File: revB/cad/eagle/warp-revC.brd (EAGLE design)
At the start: 46.7 x 72.8 mm, 176 parts, among them J3 QIIC connector, J4 DF40FC-20DP-0.4V(51)

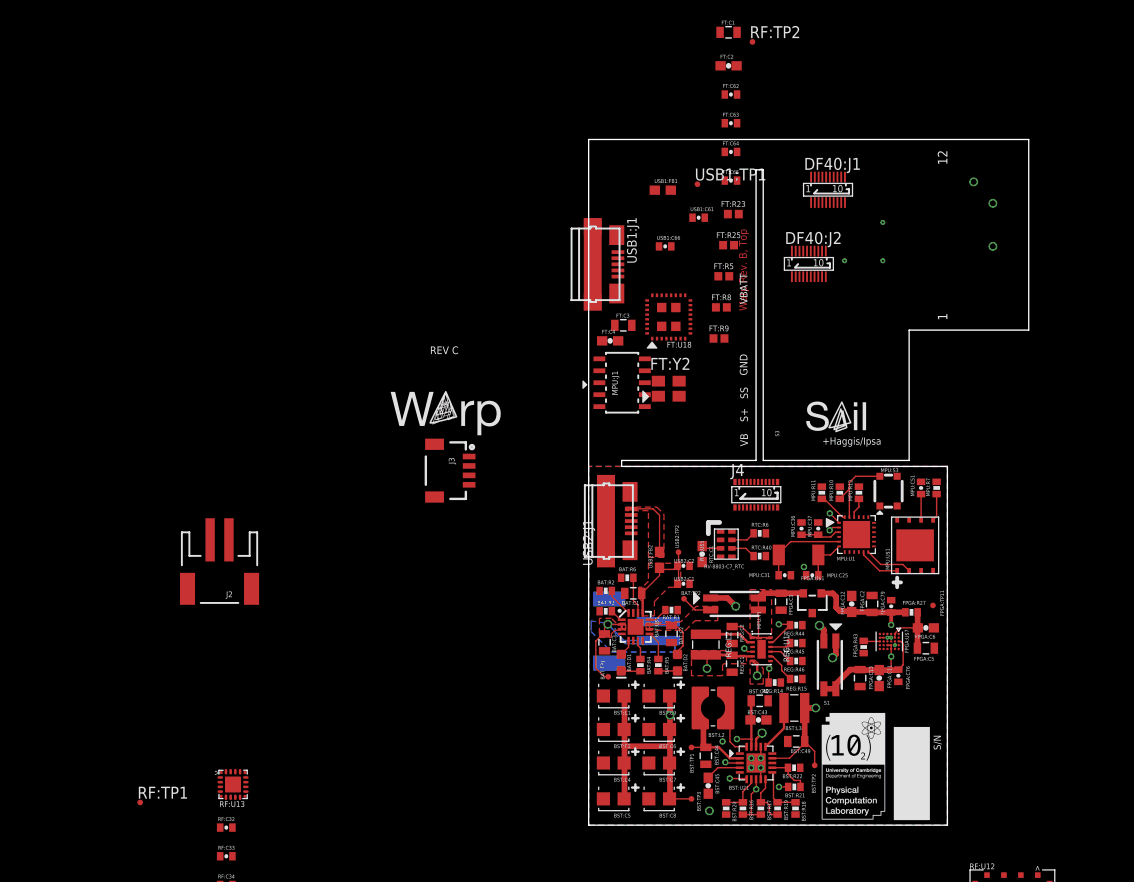
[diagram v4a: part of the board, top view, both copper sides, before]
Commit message: Top layout removed USE SPI IC
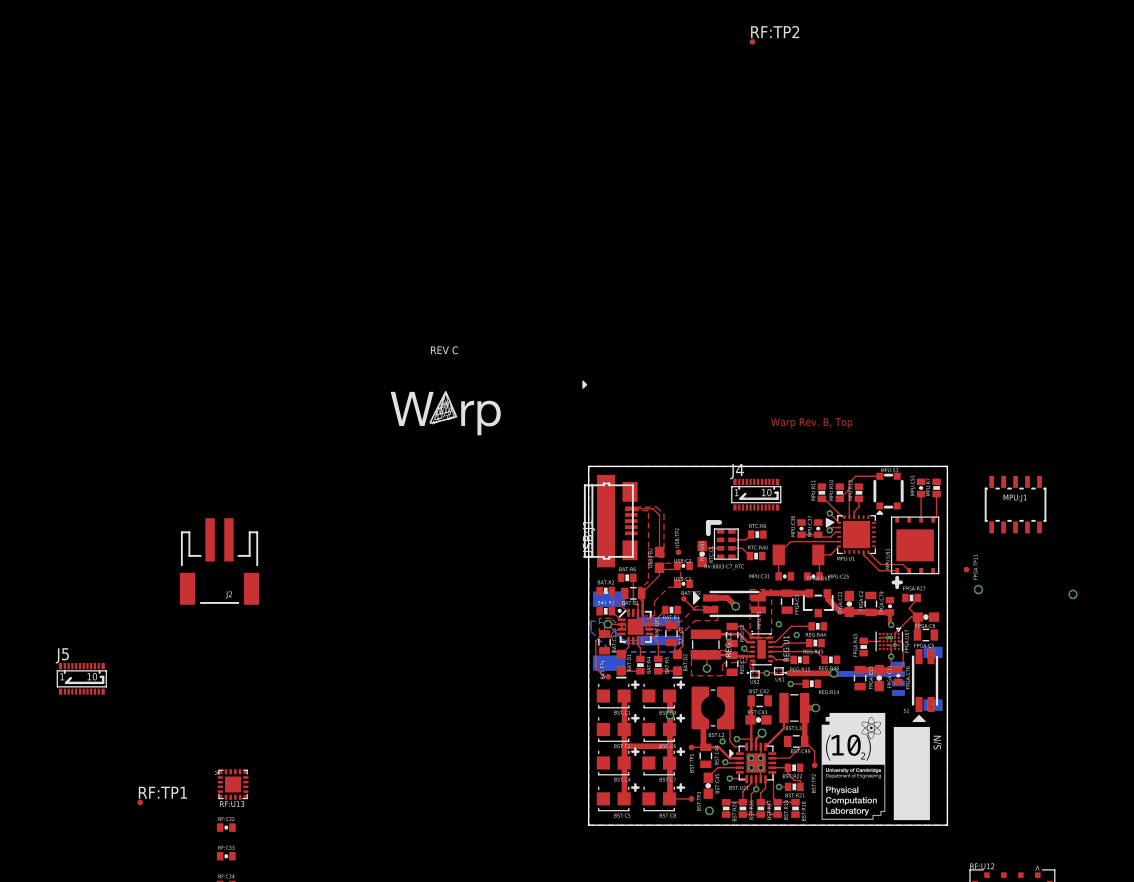
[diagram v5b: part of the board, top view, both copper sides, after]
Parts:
- removed DF40:J1, DF40:J2: DF40FC-20DP-0.4V(51)SOCKET, DF40C-20DS-0.4V(51):DF40C-20DP-0.4V(51)
- removed FT:C1, FT:C3: 4.7uF, SparkFun-Passives:0805
- removed FT:C2, FT:C4: 0.1uF, SparkFun-Passives:0603-CAP
- removed FT:C62: 0.47uF, SparkFun-Passives:0402-CAP
- removed FT:C63: 100pF, SparkFun-Passives:0402-CAP
- removed FT:C64, FT:C65: 27pF, SparkFun-Passives:0402-CAP
- removed FT:R23, FT:R25, FT:R5, FT:R8, FT:R9: (no value), SparkFun-Resistors:0402
- removed FT:U18: FT4222H, FT4222H:FT4222H
- removed FT:Y2: CS325, CS325:CS325
- removed USB1:C61: 4.7uF (pol), SparkFun-Passives:0402-CAP
- removed USB1:C66: 0.1uF, SparkFun-Passives:0402-CAP
- removed USB1:FB1: 600R/1A, SparkFun-Passives:0603
- removed USB1:J1: J_USB_MICROAB_HIROSE_ZX62-AB-5PA, j_usb_hirose_zx62-ab-5pa:J_USB_MICROAB_HIROSE_ZX62-AB-5PA
- removed USB1:TP1: TPSTP06R, testpad:TP06R
- added J5: DF40FC-20DP-0.4V(51), DF40FC-20DP-0.4V(51):DF40C-20DP-0.4V(51)
- added U$1, U$2: MAX40200, MAX40200:DSBGA
- moved J3 50.7 mm to (32.9, 15.6), flipped to the bottom
- moved MPU:J1 43.7 mm to (45.3, 34.0), turned to 0 degrees
- moved S1 12.8 mm to (37.0, 15.4), turned to 0 degrees
- moved FPGA:TP11 5.21 mm to (40.1, 27.1)
- moved REG:R14 3.94 mm to (23.7, 15.0)
- moved REG:R46 3.69 mm to (25.7, 17.6)
- moved REG:R44 2.29 mm to (24.3, 21.1)
- moved REG:R15 2.07 mm to (22.4, 17.6)
- moved REG:R45 2.03 mm to (24.1, 19.3)
- moved FPGA:R27 1.52 mm to (34.3, 24.1)
- moved FPGA:C5 1.40 mm to (35.8, 20.2)
- moved FPGA:C6 1.14 mm to (35.8, 22.1)
- moved FPGA:U$1 0.64 mm to (24.4, 23.6)
- moved FPGA:C1 0.63 mm to (21.1, 23.7)
- moved RTC:R40 0.38 mm to (17.8, 28.6)
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- renumbered USB2:C1 to USB:C1, USB2:C2 to USB:C2, USB2:FB2 to USB:FB2, USB2:J1 to USB:J1, USB2:TP2 to USB:TP2
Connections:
- net USB2:DM renamed USB:DM
- net USB2:DP renamed USB:DP
- net USB2:VBUS renamed USB:VBUS
- removed net DF40:P10A: DF40:J1.P$10
- removed net DF40:P10B: DF40:J2.P$10
- removed net DF40:P11A: DF40:J1.P$11
- removed net DF40:P11B: DF40:J2.P$11
- removed net DF40:P12A: DF40:J1.P$12
- removed net DF40:P12B: DF40:J2.P$12
- removed net DF40:P13A: DF40:J1.P$13
- removed net DF40:P13B: DF40:J2.P$13
- removed net DF40:P14A: DF40:J1.P$14
- removed net DF40:P14B: DF40:J2.P$14
- removed net DF40:P15A: DF40:J1.P$15
- removed net DF40:P15B: DF40:J2.P$15
- removed net DF40:P16A: DF40:J1.P$16
- removed net DF40:P16B: DF40:J2.P$16
- removed net DF40:P17A: DF40:J1.P$17
- removed net DF40:P17B: DF40:J2.P$17
- removed net DF40:P18A: DF40:J1.P$18
- removed net DF40:P18B: DF40:J2.P$18
- removed net DF40:P19A: DF40:J1.P$19
- removed net DF40:P19B: DF40:J2.P$19
- removed net DF40:P1A: DF40:J1.P$1
- removed net DF40:P1B: DF40:J2.P$1
- removed net DF40:P20A: DF40:J1.P$20
- removed net DF40:P20B: DF40:J2.P$20
- removed net DF40:P2A: DF40:J1.P$2
- removed net DF40:P2B: DF40:J2.P$2
- removed net DF40:P3A: DF40:J1.P$3
- removed net DF40:P3B: DF40:J2.P$3
- removed net DF40:P4A: DF40:J1.P$4
- removed net DF40:P4B: DF40:J2.P$4
- removed net DF40:P5A: DF40:J1.P$5
- removed net DF40:P5B: DF40:J2.P$5
- removed net DF40:P6A: DF40:J1.P$6
- removed net DF40:P6B: DF40:J2.P$6
- removed net DF40:P7A: DF40:J1.P$7
- removed net DF40:P7B: DF40:J2.P$7
- removed net DF40:P8A: DF40:J1.P$8
- removed net DF40:P8B: DF40:J2.P$8
- removed net DF40:P9A: DF40:J1.P$9
- removed net DF40:P9B: DF40:J2.P$9
- removed net FT:FT4222_VOUT3V3: FT:C3.1, FT:C4.1, FT:U18.P$25
- removed net FT:N$15: FT:C65.1, FT:R25.2, FT:U18.P$19, FT:Y2.1
- removed net FT:N$2: FT:R23.2, FT:U18.P$32
- removed net FT:N$3: FT:R8.2, FT:U18.P$2
- removed net FT:N$4: FT:C62.1, FT:R5.1, FT:U18.P$3
- removed net FT:N$5: FT:C63.1, FT:R9.2, FT:U18.P$21
- removed net FT:N$6: FT:C64.1, FT:R25.1, FT:U18.P$18, FT:Y2.3
- removed net FT:VPP: FT:U18.P$29
- removed net USB1:VBUS: USB1:FB1.2, USB1:J1.P$1
- removed net USB_DM: FT:U18.P$22, USB1:J1.P$2
- removed net USB_DP: FT:U18.P$23, USB1:J1.P$3
- new net REG_LOAD: REG:U1.6, U$2.A1
- new net VCC_QIIC: J3.2, U$1.A1
- net ADXL362_FT4222_SPI_CS: no longer FT:U18.P$17
- net GND: now also U$1.B2, U$2.B2; no longer FT:C1.2, FT:C2.2, FT:C3.2, FT:C4.2, FT:C62.2, FT:C63.2, FT:C64.2, FT:C65.2, FT:R9.1, FT:U18.P$20, FT:U18.P$24, FT:U18.P$27, FT:U18.P$28, FT:U18.P$4, FT:U18.P$5, FT:U18.P$6, USB1:C61.2, USB1:C66.2, USB1:J1.P$5, USB1:J1.SHIELD1, USB1:J1.SHIELD2, USB1:J1.SHIELD3, USB1:J1.SHIELD4
- net I2C0_SCL/UART_TX: no longer FT:U18.P$13
- net I2C0_SDA/UART_RX: no longer FT:U18.P$14
- net ISL23415_SPI_CS/FT4222_GPIO3: no longer FT:U18.P$16
- net SI4705_!RST!/FT4222_GPIO2: no longer FT:U18.P$15
- net SPI_MISO/UART_RTS: no longer FT:U18.P$9
- net SPI_MOSI/UART_CTS: no longer FT:U18.P$10
- net SPI_SCK: no longer FT:U18.P$8
- net USB_5V: no longer FT:C1.1, FT:C2.1, FT:U18.P$26, FT:U18.P$30, USB1:C61.1, USB1:C66.1, USB1:FB1.1, USB1:TP1.TP
- net VS1: no longer FT:R23.1, FT:R5.2, FT:R8.1, FT:U18.P$1, FT:U18.P$7
- net VS2: now also U$1.A2, U$2.A2; no longer J3.2, REG:U1.6
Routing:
- net VCC_QIIC: track 0.00 -> 12.1 mm, vias 0 -> 1
- net REG_VSEL2: track 8.39 -> 18.0 mm
- net FPGA_VS: track 17.9 -> 12.9 mm
- net USB_5V: track 11.2 -> 6.98 mm
- net REG_VSEL3: track 2.49 -> 6.13 mm
- net REG_CTRL: track 6.06 -> 9.11 mm
- net FPGA:VCC_1V2: track 13.2 -> 10.7 mm
- net VS1: track 17.7 -> 15.8 mm
- net VS2: track 3.60 -> 2.19 mm
- net REG_VSEL1: track 19.5 -> 20.8 mm
- net FPGA:ICE40_VCC_PLL: track 6.98 -> 8.27 mm
- net REG_LOAD: track 0.00 -> 1.28 mm
- net REG_VSEL4: track 3.39 -> 2.62 mm
- net REG_VIN: track 14.7 -> 15.4 mm
- net GND: vias 10 -> 7
- added copper zone on layer 1, net REG_LOAD
- removed copper zone on layer 5, net ICE40_VCC_1V2
- removed copper zone on layer 1, net VS2
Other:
- board size 46.7 x 72.8 mm -> 38.1 x 38.1 mm
- board text removed: "+Haggis/Ipsa"
- board text removed: "1"
- board text removed: "12"
- board text removed: "20"
- board text removed: "4"
- board text removed: "GND"
- board text removed: "S+"
- board text removed: "SS"
- board text removed: "VB"
- board text removed: "VBATT"

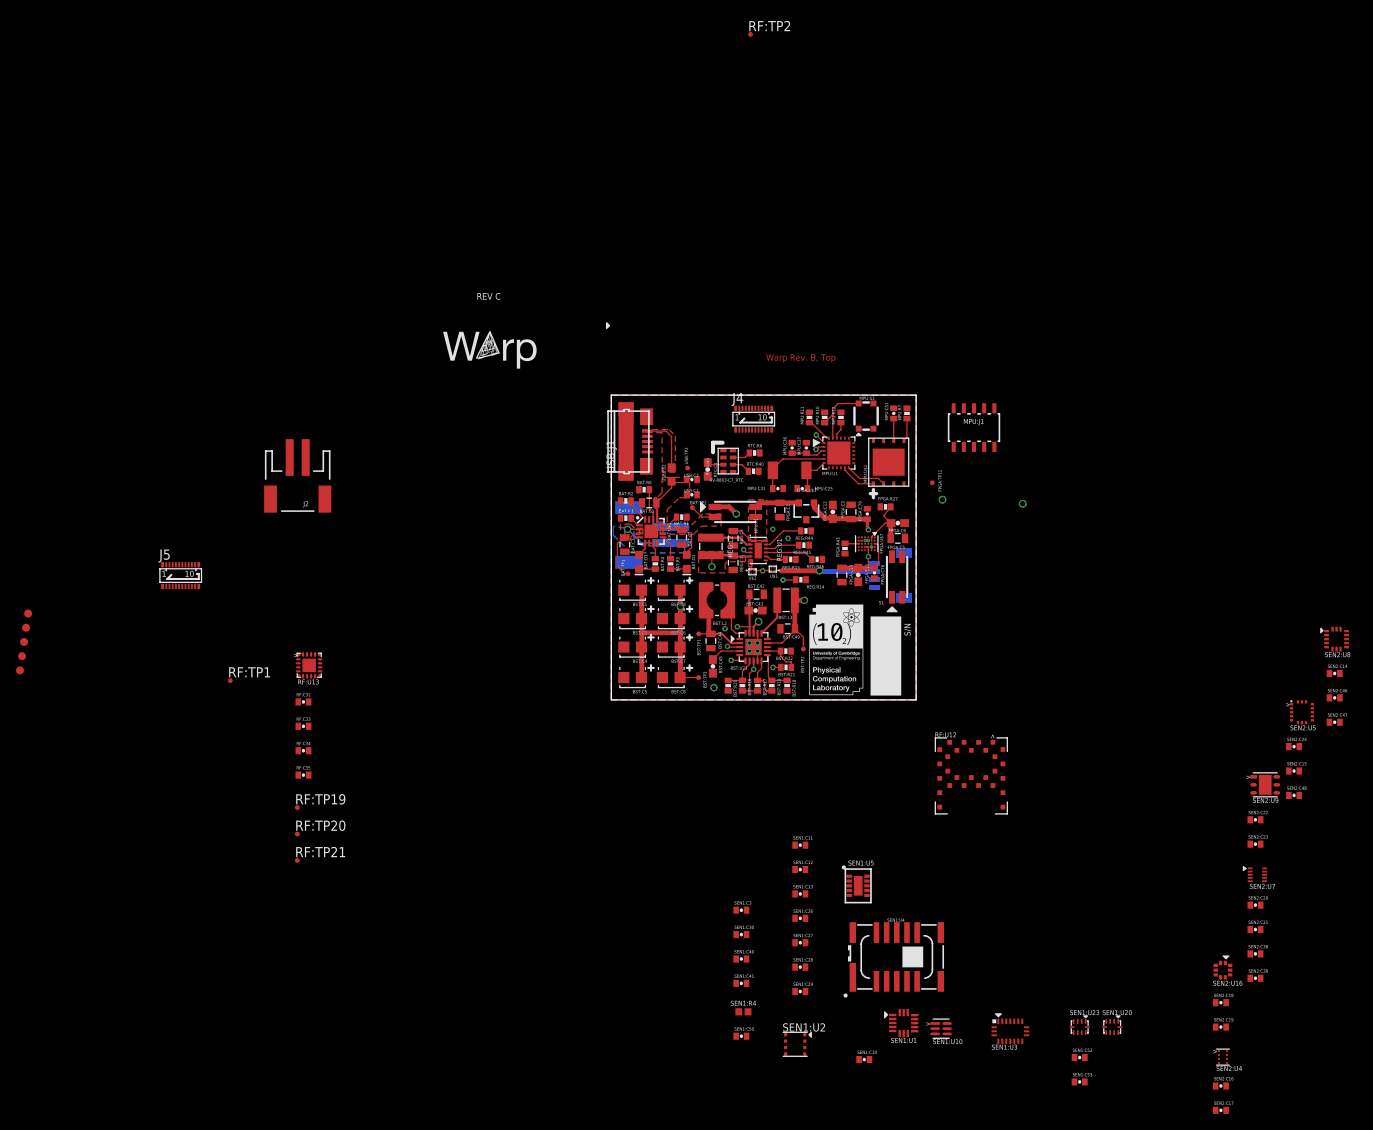
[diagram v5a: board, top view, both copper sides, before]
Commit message: Start of bottom layer sensor routing
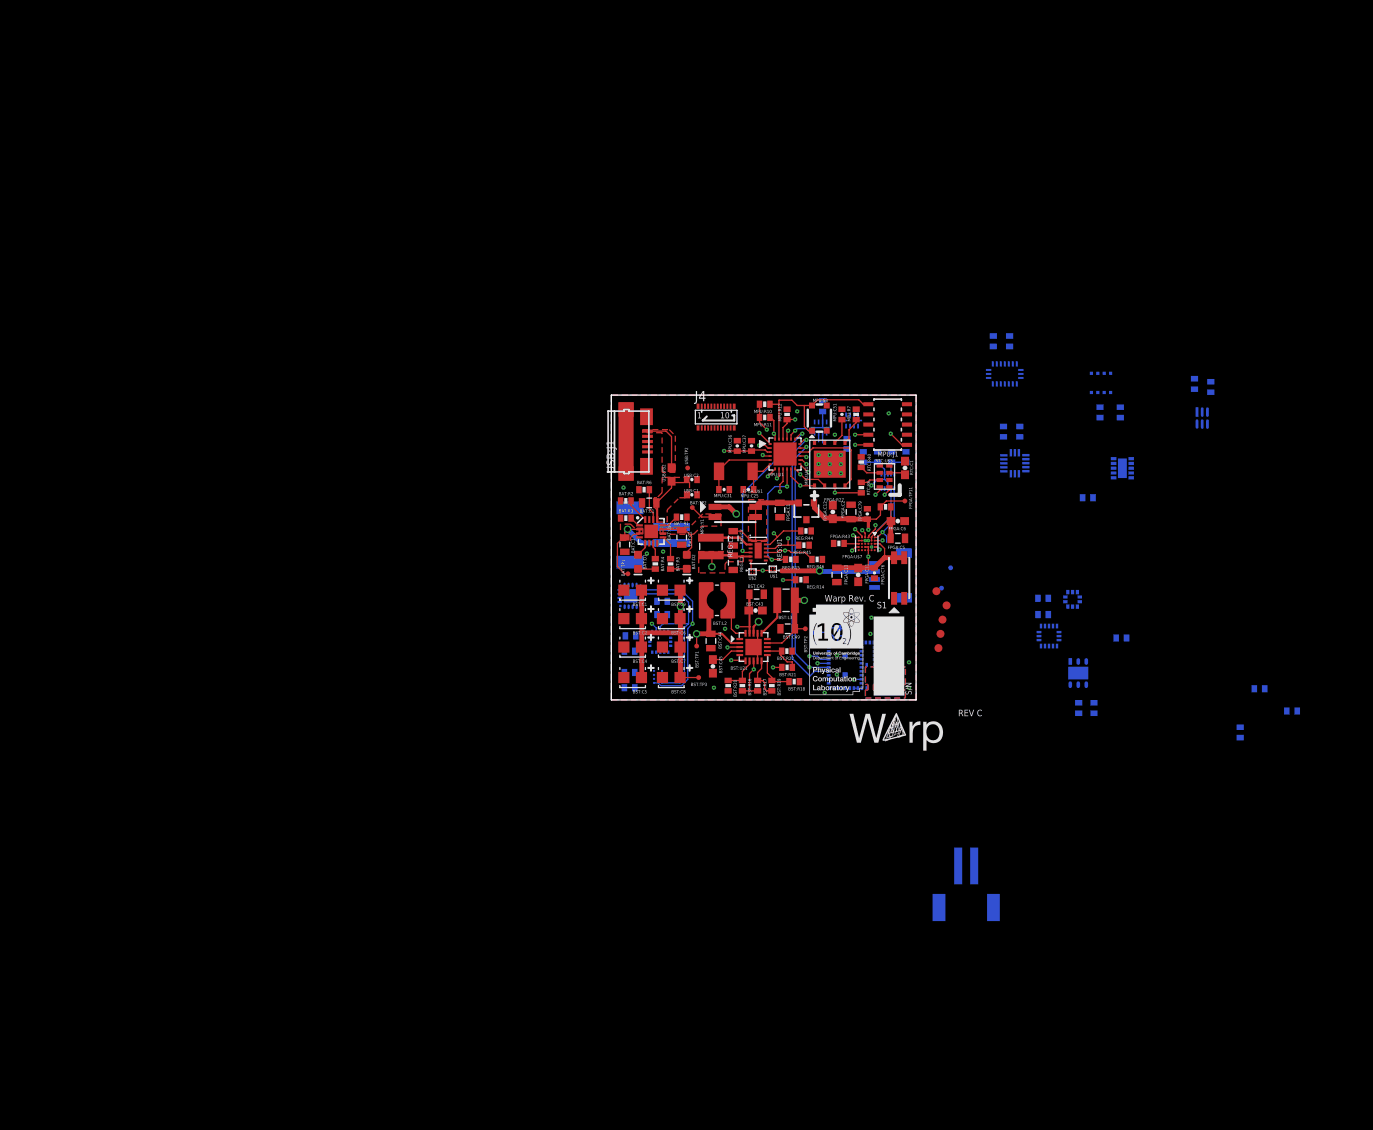
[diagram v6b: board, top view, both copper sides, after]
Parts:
- removed J5: DF40FC-20DP-0.4V(51), DF40FC-20DP-0.4V(51):DF40C-20DP-0.4V(51)
- removed RF:C32, RF:C34, SEN1:C3: 0.1uF, SparkFun-Passives:0402-CAP
- removed RF:C33, SEN1:C30: 10uF, SparkFun-Passives:0402-CAP
- removed RF:C35: 22nF, SparkFun-Passives:0402-CAP
- removed RF:TP1, RF:TP19, RF:TP2, RF:TP20, RF:TP21: TPTP06R, testpad:TP06R
- removed RF:U12: PAN1326C, PAN1326B:PAN1326B
- removed RF:U13: SI4705, SI4705:SI4705
- removed SEN1:C40: 2.2uF, SparkFun-Passives:0402-CAP
- removed SEN1:C41: 1.0uF, SparkFun-Passives:0402-CAP
- removed SEN1:R4: 20, SparkFun-Resistors:0402
- removed SEN1:U4: GRIDEYE, SparkFun-Sensors:GRIDEYE-AMG88
- added BT:C1: 1uF, SparkFun-Passives:0603-CAP
- added BT:C32, SEN2:C34: 0.1uF, SparkFun-Passives:0402-CAP
- added BT:U1: BGX13S, BGX13S:BGX13S
- added BT:Y1: IQXC-25, IQXC-25:IQXC-25
- added SEN2:C35: 22nF, SparkFun-Passives:0402-CAP
- added SEN2:TP1, SEN2:TP2: TPTP06R, testpad:TP06R
- added SEN2:U13: SI4705, SI4705:SI4705
- moved FD3 115.1 mm to (41.9, 11.8)
- moved FD5 114.8 mm to (41.4, 10.0)
- moved FD2 114.8 mm to (41.1, 8.26)
- moved FD4 114.8 mm to (40.9, 6.48)
- moved FD1 113.6 mm to (40.6, 13.6)
- moved J2 97.9 mm to (44.4, -24.5), flipped to the bottom
- moved SEN2:C17 92.0 mm to (2.29, 3.43), flipped to the bottom
- moved SEN1:U2 91.1 mm to (61.2, 39.6), flipped to the bottom, turned to 90 degrees
- moved SEN1:C29 90.5 mm to (72.9, 39.5), flipped to the bottom, turned to 90 degrees
- moved SEN1:C53 90.4 mm to (26.4, 36.7), flipped to the bottom, turned to 90 degrees
- moved SEN2:C16 89.1 mm to (2.29, 1.52), flipped to the bottom
- moved SEN1:C28 88.8 mm to (74.9, 39.1), flipped to the bottom, turned to 90 degrees
- moved SEN2:U4 85.2 mm to (5.84, 2.92), flipped to the bottom, turned to 180 degrees
- moved SEN2:C48 85.0 mm to (2.29, 6.10), flipped to the bottom
- moved SEN2:C15 84.6 mm to (2.41, 8.00), flipped to the bottom
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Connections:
- net ADXL362_FT4222_SPI_CS renamed ADXL362_SPI_CS
- net ISL23415_SPI_CS/FT4222_GPIO3 renamed ISL23415_SPI_CS
- removed net KL03_CLKOUT32K: MPU:U1.P$21, RF:U12.P$8, RF:U13.P$9
- removed net PAN1326_!SHUTD: J4.P$20, MPU:U1.P$13, RF:U12.P$16
- removed net RF:PAN1326_AUD_CLK: RF:U12.P$19, RF:U13.P$17
- removed net RF:PAN1326_AUD_FSYNC: RF:U12.P$7, RF:U13.P$16
- removed net RF:PAN1326_AUD_IN: RF:U12.P$18, RF:U13.P$15
- removed net RF:PAN1326_AUD_OUT: RF:TP20.TP, RF:U12.P$17
- removed net RF:PAN1326_RF: RF:TP21.TP, RF:U12.P$13
- removed net RF:PAN1326_TX_DBG: RF:TP19.TP, RF:U12.P$2
- removed net RF:SI4705_LPI: RF:TP1.TP, RF:U13.P$4
- removed net SEN1:AVDD: SEN1:C41.1, SEN1:U4.10
- removed net SEN1:DVDD: SEN1:C40.1, SEN1:U4.12
- removed net SEN1:N$1: SEN1:C41.2, SEN1:R4.2
- removed net SI4705_!RST!/FT4222_GPIO2: J4.P$19, MPU:U1.P$14, RF:U13.P$5
- removed net SI4705_FMI: RF:TP2.TP, RF:U13.P$2
- new net BGX13S_!RST: BT:U1.44, J4.P$20, MPU:U1.P$7
- new net BT:N$1: BT:U1.21, BT:Y1.1
- new net BT:N$2: BT:U1.19, BT:Y1.2
- new net BT:N$3: BT:U1.2, BT:U1.3
- new net CLK32K: MPU:U1.P$21, SEN2:U13.P$9
- new net SEN2:SI4705_FMI: SEN2:TP2.TP, SEN2:U13.P$2
- new net SEN2:SI4705_LPI: SEN2:TP1.TP, SEN2:U13.P$4
- new net SI4705_!RST: J4.P$19, SEN2:U13.P$5
- new net SI4705_!RST!: MPU:U1.P$14
- net FPGA_CS: now also MPU:U1.P$13; no longer MPU:U1.P$7
- net GND: now also BT:C1.2, BT:C32.2, BT:U1.1, BT:U1.20, BT:U1.31, BT:U1.4, BT:U1.45, BT:U1.46, BT:U1.47, BT:U1.48, BT:U1.49, BT:U1.5, BT:U1.50, BT:U1.51, SEN2:C34.2, SEN2:C35.2, SEN2:U13.P$12, SEN2:U13.P$21, SEN2:U13.P$3, SEN2:U13.P$6; no longer RF:C32.2, RF:C33.2, RF:C34.2, RF:C35.2, RF:U12.P$1, RF:U12.P$12, RF:U12.P$14, RF:U12.P$20, RF:U13.P$12, RF:U13.P$21, RF:U13.P$3, RF:U13.P$6, SEN1:C3.2, SEN1:C30.2, SEN1:C40.2, SEN1:R4.1, SEN1:U4.5, SEN1:U4.6
- net I2C0_SCL/UART_TX: now also BT:U1.14; no longer RF:U12.P$5
- net I2C0_SDA/UART_RX: now also BT:U1.13; no longer RF:U12.P$6
- net I2C1_SCL: no longer SEN1:U4.3
- net I2C1_SDA: no longer SEN1:U4.2
- net I2C2_SCL: now also SEN2:U13.P$7; no longer RF:U13.P$7
- net I2C2_SDA: now also SEN2:U13.P$8; no longer RF:U13.P$8
- net SPI_MISO/UART_RTS: now also BT:U1.16; no longer RF:U12.P$4
- net SPI_MOSI/UART_CTS: now also BT:U1.15; no longer RF:U12.P$3
- net VS2: now also BT:C1.1, BT:C32.1, BT:U1.22, BT:U1.24, SEN2:C34.1, SEN2:C35.1, SEN2:U13.P$10, SEN2:U13.P$11; no longer RF:C32.1, RF:C33.1, RF:C34.1, RF:C35.1, RF:U12.P$10, RF:U12.P$11, RF:U12.P$15, RF:U12.P$22, RF:U13.P$10, RF:U13.P$11, SEN1:C3.1, SEN1:C30.1, SEN1:U4.13, SEN1:U4.9
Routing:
- net SPI_MOSI/UART_CTS: track 0.02 -> 39.0 mm, vias 0 -> 3
- net I2C0_SDA/UART_RX: track 0.00 -> 36.0 mm, vias 0 -> 2
- net I2C2_SCL: track 0.00 -> 35.2 mm, vias 0 -> 3
- net I2C0_SCL/UART_TX: track 0.00 -> 33.3 mm, vias 0 -> 3
- net I2C2_SDA: track 0.00 -> 32.2 mm, vias 0 -> 1
- net BGX13S_!RST: track 0.00 -> 32.1 mm, vias 0 -> 2
- net SPI_MISO/UART_RTS: track 4.57 -> 36.5 mm, vias 0 -> 3
- net VS2: track 2.19 -> 22.3 mm, vias 2 -> 3
- net REG_CTRL: track 9.11 -> 28.2 mm, vias 2 -> 3
- net FPGA_CS: track 0.00 -> 14.5 mm, vias 0 -> 2
- net RTC_!INT!/RESET_B: track 10.9 -> 24.7 mm
- net REG_VSEL4: track 2.62 -> 16.1 mm, vias 0 -> 2
- net SWD_DIO: track 3.24 -> 16.3 mm, vias 0 -> 2
- net VS1: track 15.8 -> 28.3 mm, vias 2 -> 5
- net REG_VSEL3: track 6.13 -> 17.8 mm, vias 0 -> 2
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- added copper zone on layer 1, net ANT_CLEAR
- added copper zone on layer 14, net ANT_CLEAR
- added copper zone on layer 15, net ANT_CLEAR
- added copper zone on layer 16, net ANT_CLEAR
- added copper zone on layer 2, net ANT_CLEAR
- added copper zone on layer 3, net ANT_CLEAR
- added copper zone on layer 4, net ANT_CLEAR
- added copper zone on layer 5, net ANT_CLEAR
- added copper zone on layer 6, net ANT_CLEAR
- added copper zone on layer 7, net ANT_CLEAR
- added copper zone on layer 16, net GND
- removed copper zone on layer 16, net BAT
- removed copper zone on layer 1, net REG_LOAD
- removed copper zone on layer 16, net VS2
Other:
- board text added: "Warp Rev. C"
- board text removed: "Designed by PSM in Cambridge, MA/UK"
- board text removed: "Warp Rev. B, Top"
